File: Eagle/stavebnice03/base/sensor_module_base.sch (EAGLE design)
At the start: 5 parts

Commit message: I did an order in Eagle files
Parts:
- added C1, C3, C4, C5: 100nF, resistor:C-EUC0603
- added R1, R2, R4: 2k2, resistor:R-EU_R0603
- added R3: 2K2, resistor:R-EU_R0603
- added U$2, U$3, U$6, U$7: NC7SB3157P6X, !stavebnice03:NC7SB3157P6X
- added U$5: JUMPER5F-90, !stavebnice03:JUMPER5F-90
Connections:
- new net N$1: U$1.RA4, U$6.S, U$7.S
- new net N$10: R2.1, U$5.2, U$6.B0, U$7.B1
- new net N$20: U$2.B0, U$7.A
- new net N$4: U$1.RC1, U$3.A
- new net N$6: R1.1, U$5.4, U$6.B1, U$7.B0
- new net N$7: U$3.B0, U$6.A
- new net N$8: R4.1, U$3.B1, U$4.2
- new net N$9: U$1.RA5, U$2.S, U$3.S
- net GND: now also C1.2, C3.1, C4.2, C5.1, U$2.GND, U$3.GND, U$5.1, U$5.5, U$6.GND, U$7.GND
- net N$2: now also U$2.A; no longer U$4.2
- net N$5: now also R3.1, U$2.B1; no longer U$1.RC1
- net VCC: now also C1.1, C3.2, C4.1, C5.2, R1.2, R2.2, R3.2, R4.2, U$2.VCC, U$3.VCC, U$5.3, U$6.VCC, U$7.VCC; no longer U$1.RA4, U$1.RA5

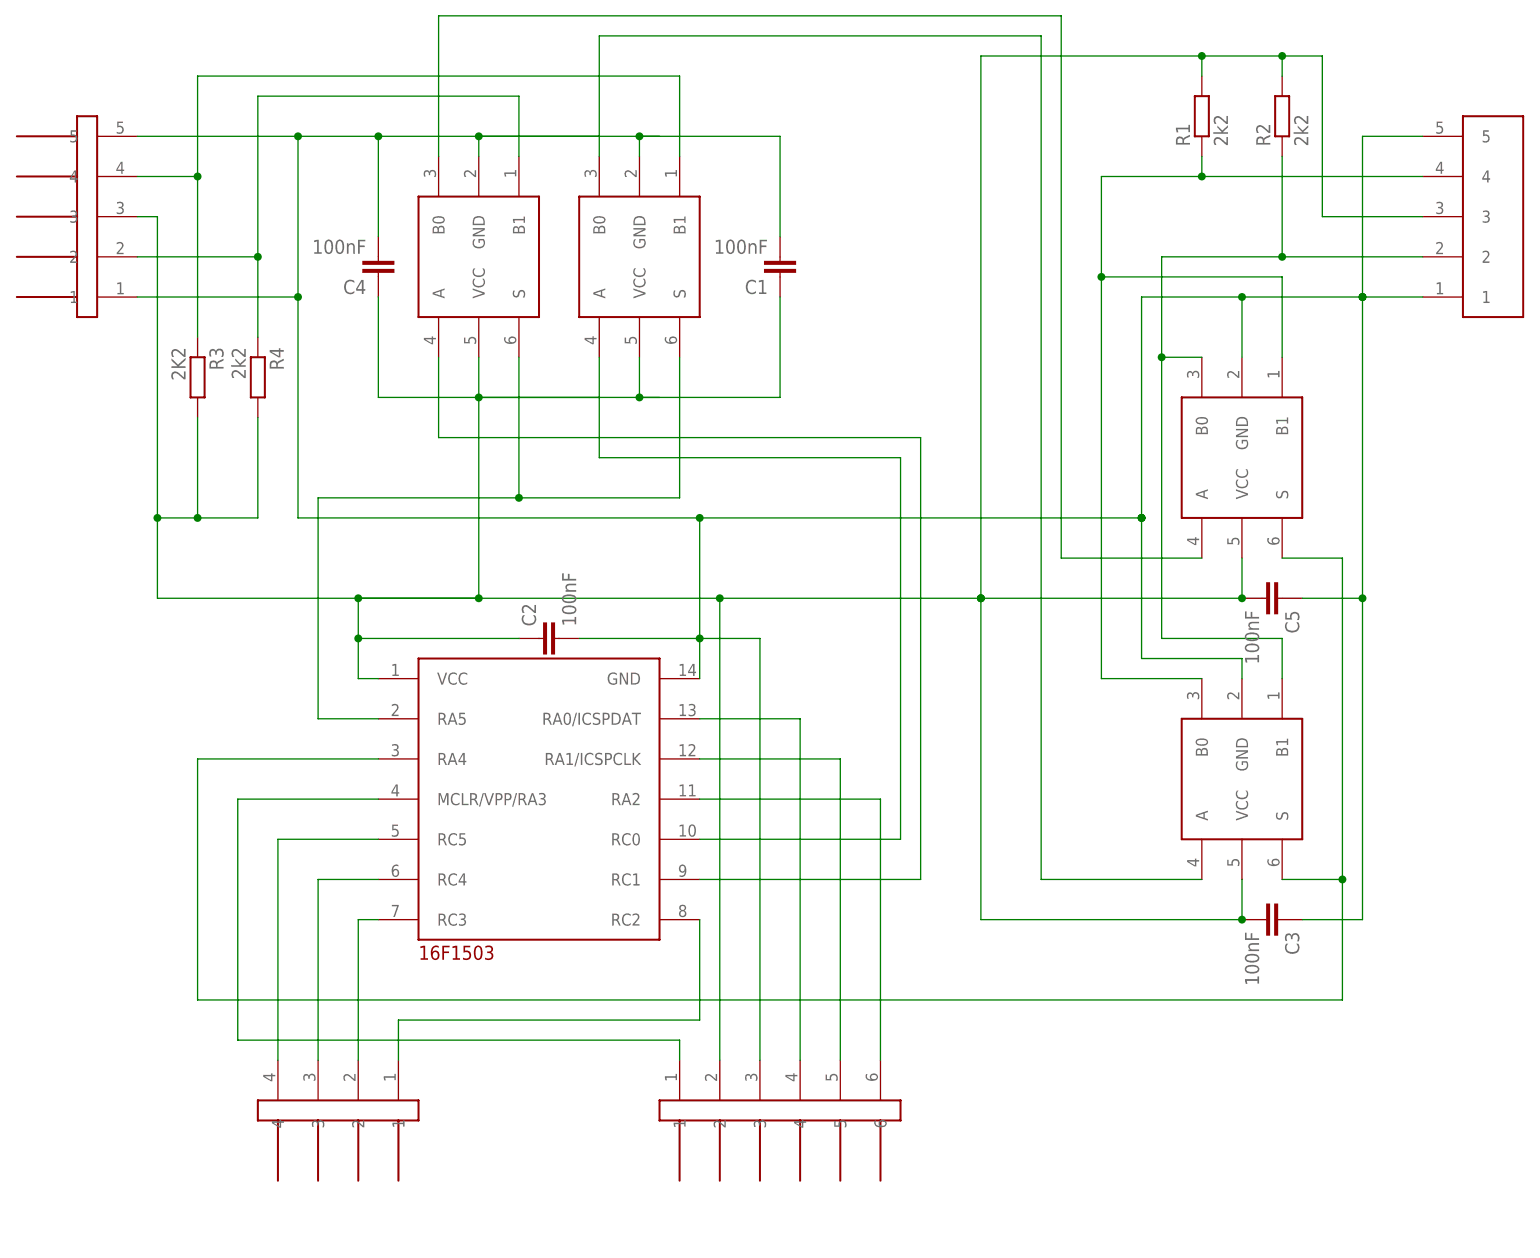
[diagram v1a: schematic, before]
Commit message: added wire from input bus to an iterrupt pin
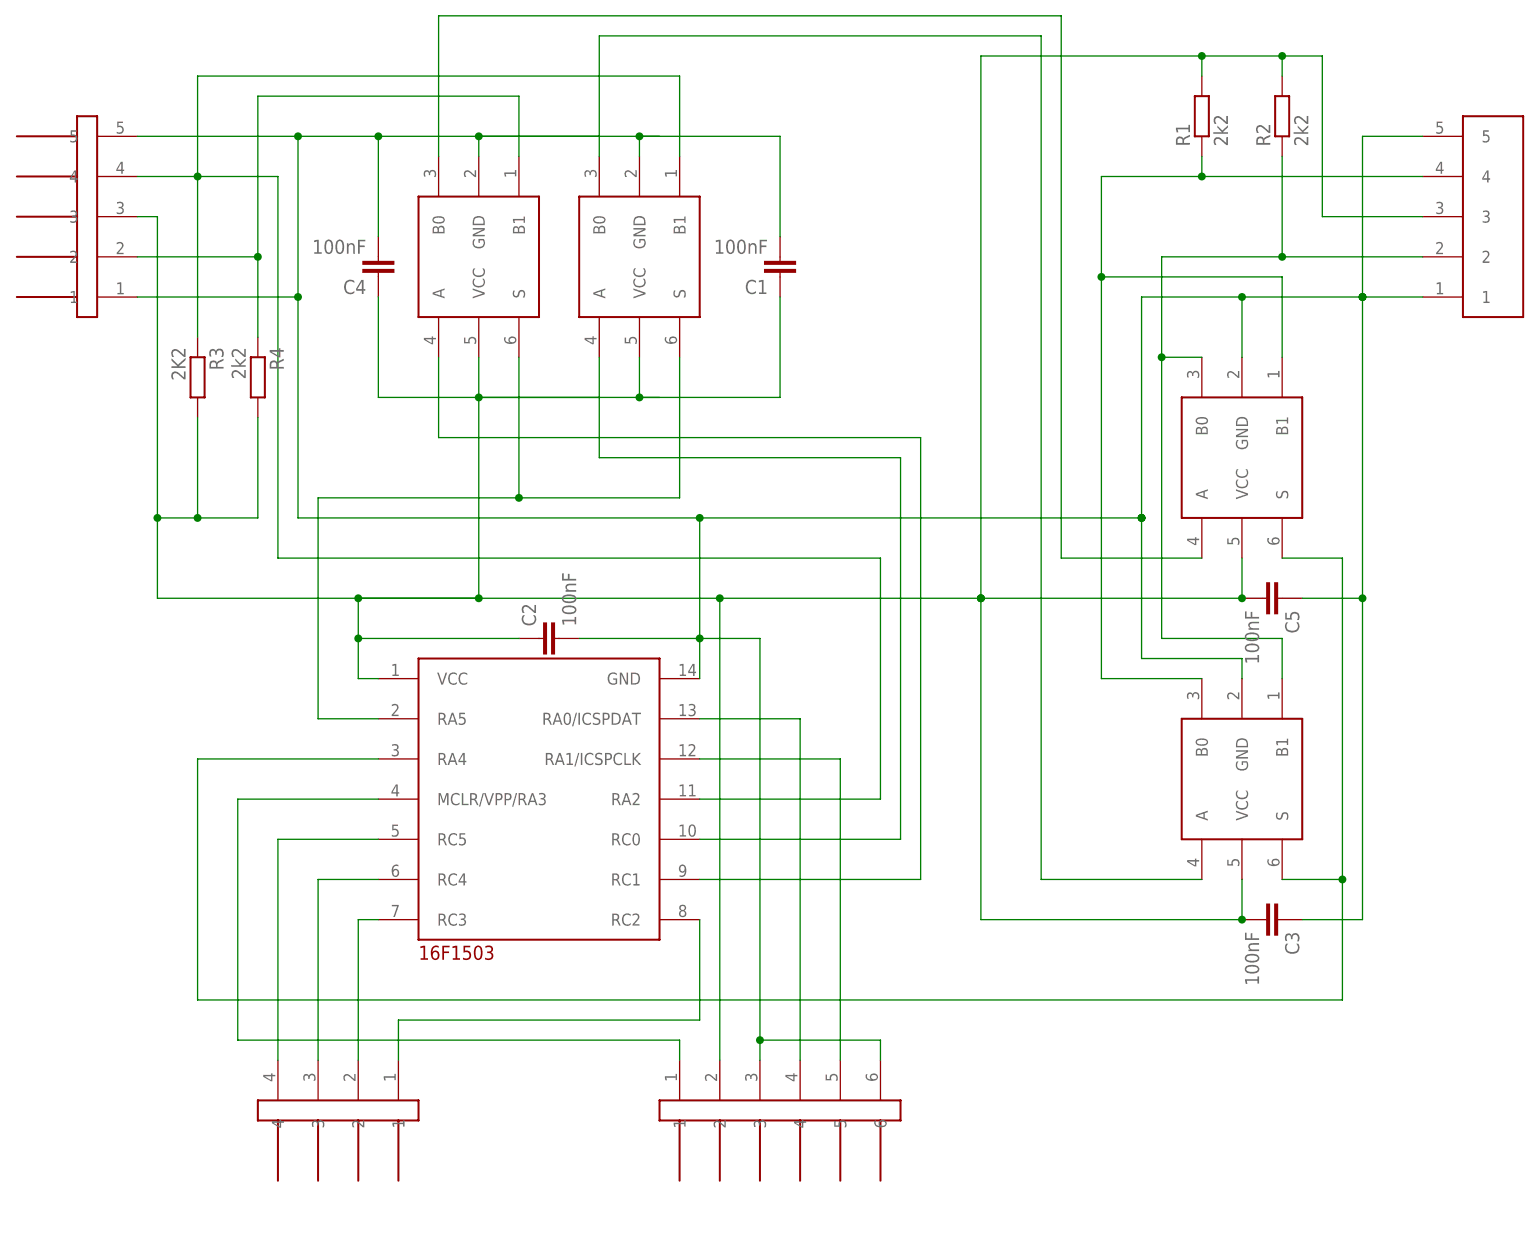
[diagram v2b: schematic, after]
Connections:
- removed net N$5: R3.1, U$2.B1, U$4.4
- net GND: now also U$8.6
- net N$11: now also R3.1, U$2.B1, U$4.4; no longer U$8.6
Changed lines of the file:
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@@
 <wire x1="124.46" y1="167.64" x2="124.46" y2="154.94" width="0.1524" layer="91"/>
 <junction x="137.16" y="167.64"/>
-<wire x1="172.72" y1="50.8" x2="172.72" y2="104.14" width="0.1524" layer="91"/>
+<wire x1="172.72" y1="50.8" x2="172.72" y2="53.34" width="0.1524" layer="91"/>
+<wire x1="172.72" y1="53.34" x2="172.72" y2="104.14" width="0.1524" layer="91"/>
 <wire x1="165.1" y1="104.14" x2="172.72" y2="104.14" width="0.1524" layer="91"/>
 <pinref part="U$1" gate="G$1" pin="GND"/>
@@
 <junction x="124.46" y="167.64"/>
 <junction x="114.3" y="167.64"/>
+<pinref part="U$8" gate="G$1" pin="6"/>
+<wire x1="172.72" y1="53.34" x2="187.96" y2="53.34" width="0.1524" layer="91"/>
+<wire x1="187.96" y1="53.34" x2="187.96" y2="50.8" width="0.1524" layer="91"/>
+<junction x="172.72" y="53.34"/>
 </segment>
 </net>
@@
 <pinref part="U$1" gate="G$1" pin="RA2"/>
 <wire x1="165.1" y1="83.82" x2="187.96" y2="83.82" width="0.1524" layer="91"/>
-<wire x1="187.96" y1="83.82" x2="187.96" y2="50.8" width="0.1524" layer="91"/>
-<pinref part="U$8" gate="G$1" pin="6"/>
+<wire x1="187.96" y1="83.82" x2="187.96" y2="114.3" width="0.1524" layer="91"/>
+<wire x1="187.96" y1="114.3" x2="111.76" y2="114.3" width="0.1524" layer="91"/>
+<wire x1="111.76" y1="114.3" x2="111.76" y2="162.56" width="0.1524" layer="91"/>
+<wire x1="162.56" y1="165.1" x2="162.56" y2="175.26" width="0.1524" layer="91"/>
+<pinref part="U$2" gate="G$1" pin="B1"/>
+<pinref part="U$4" gate="G$1" pin="4"/>
+<wire x1="162.56" y1="175.26" x2="101.6" y2="175.26" width="0.1524" layer="91"/>
+<wire x1="101.6" y1="162.56" x2="93.98" y2="162.56" width="0.1524" layer="91"/>
+<pinref part="R3" gate="G$1" pin="1"/>
+<wire x1="101.6" y1="175.26" x2="101.6" y2="162.56" width="0.1524" layer="91"/>
+<wire x1="101.6" y1="162.56" x2="101.6" y2="142.24" width="0.1524" layer="91"/>
+<junction x="101.6" y="162.56"/>
+<wire x1="111.76" y1="162.56" x2="101.6" y2="162.56" width="0.1524" layer="91"/>
 </segment>
 </net>
@@
 </segment>
 </net>
-<net name="N$5" class="0">
-<segment>
-<wire x1="162.56" y1="165.1" x2="162.56" y2="175.26" width="0.1524" layer="91"/>
-<pinref part="U$2" gate="G$1" pin="B1"/>
-<pinref part="U$4" gate="G$1" pin="4"/>
-<wire x1="162.56" y1="175.26" x2="101.6" y2="175.26" width="0.1524" layer="91"/>
-<wire x1="101.6" y1="162.56" x2="93.98" y2="162.56" width="0.1524" layer="91"/>
-<pinref part="R3" gate="G$1" pin="1"/>
-<wire x1="101.6" y1="175.26" x2="101.6" y2="162.56" width="0.1524" layer="91"/>
-<wire x1="101.6" y1="162.56" x2="101.6" y2="142.24" width="0.1524" layer="91"/>
-<junction x="101.6" y="162.56"/>
-</segment>
-</net>

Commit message: added pin and resistor to stay in bootloader + changed size back to 21x21 mm
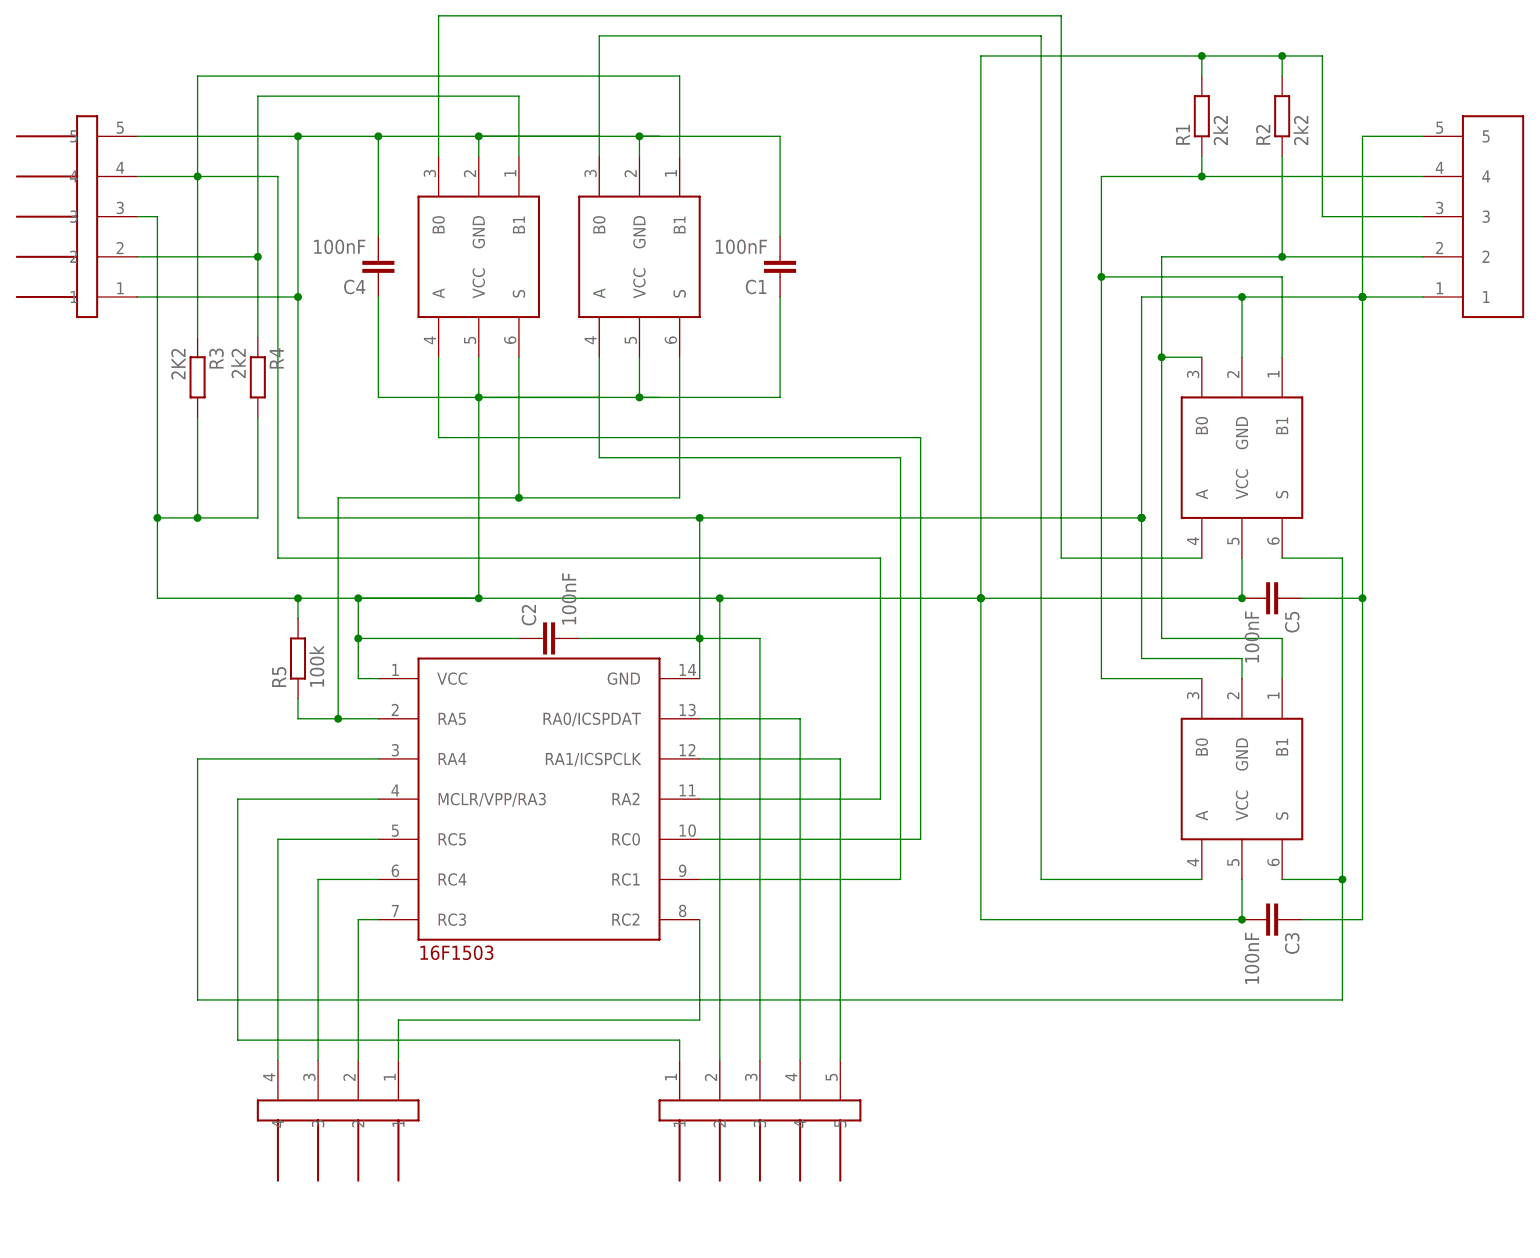
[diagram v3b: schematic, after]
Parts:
- added R5: 100k, resistor:R-EU_R0603
- U$8: value JUMPER6M -> JUMPER5M; device !stavebnice03:JUMPER6M -> !stavebnice03:JUMPER5M
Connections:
- net GND: no longer U$8.6
- net N$2: now also U$1.RC1; no longer U$1.RC0
- net N$4: now also U$1.RC0; no longer U$1.RC1
- net N$9: now also R5.1
- net VCC: now also R5.2
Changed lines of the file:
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@@
 <layer number="97" name="Info" color="7" fill="1" visible="yes" active="yes"/>
 <layer number="98" name="Guide" color="6" fill="1" visible="yes" active="yes"/>
+<layer number="99" name="SpiceOrder" color="5" fill="1" visible="no" active="no"/>
 </layers>
 <schematic xreflabel="%F%N/%S.%C%R" xrefpart="/%S.%C%R">
@@
 <part name="C5" library="resistor" deviceset="C-EU" device="C0603" value="100nF"/>
 <part name="C4" library="resistor" deviceset="C-EU" device="C0603" value="100nF"/>
-<part name="U$8" library="!stavebnice03" deviceset="JUMPER6M" device=""/>
 <part name="U$9" library="!stavebnice03" deviceset="JUMPER4M" device=""/>
 <part name="R3" library="resistor" deviceset="R-EU_" device="R0603" value="2K2"/>
 <part name="R4" library="resistor" deviceset="R-EU_" device="R0603" value="2k2"/>
+<part name="R5" library="resistor" deviceset="R-EU_" device="R0603" value="100k"/>
+<part name="U$8" library="!stavebnice03" deviceset="JUMPER5M" device=""/>
 </parts>
 <sheets>
@@
 <instance part="C5" gate="G$1" x="238.76" y="109.22" rot="R270"/>
 <instance part="C4" gate="G$1" x="124.46" y="149.86" rot="R180"/>
-<instance part="U$8" gate="G$1" x="175.26" y="43.18" rot="MR270"/>
 <instance part="U$9" gate="G$1" x="119.38" y="43.18" rot="R270"/>
 <instance part="R3" gate="G$1" x="101.6" y="137.16" rot="R270"/>
 <instance part="R4" gate="G$1" x="109.22" y="137.16" rot="R270"/>
+<instance part="R5" gate="G$1" x="114.3" y="101.6" rot="R90"/>
+<instance part="U$8" gate="G$1" x="172.72" y="43.18" rot="MR270"/>
 </instances>
 <busses>
@@
 <wire x1="124.46" y1="167.64" x2="124.46" y2="154.94" width="0.1524" layer="91"/>
 <junction x="137.16" y="167.64"/>
-<wire x1="172.72" y1="50.8" x2="172.72" y2="53.34" width="0.1524" layer="91"/>
-<wire x1="172.72" y1="53.34" x2="172.72" y2="104.14" width="0.1524" layer="91"/>
+<wire x1="172.72" y1="50.8" x2="172.72" y2="104.14" width="0.1524" layer="91"/>
 <wire x1="165.1" y1="104.14" x2="172.72" y2="104.14" width="0.1524" layer="91"/>
 <pinref part="U$1" gate="G$1" pin="GND"/>
@@
 <wire x1="157.48" y1="165.1" x2="157.48" y2="167.64" width="0.1524" layer="91"/>
 <junction x="157.48" y="167.64"/>
-<pinref part="U$8" gate="G$1" pin="3"/>
 <junction x="248.92" y="147.32"/>
 <junction x="124.46" y="167.64"/>
 <junction x="114.3" y="167.64"/>
-<pinref part="U$8" gate="G$1" pin="6"/>
-<wire x1="172.72" y1="53.34" x2="187.96" y2="53.34" width="0.1524" layer="91"/>
-<wire x1="187.96" y1="53.34" x2="187.96" y2="50.8" width="0.1524" layer="91"/>
-<junction x="172.72" y="53.34"/>
+<pinref part="U$8" gate="G$1" pin="3"/>
 </segment>
 </net>
@@
 <wire x1="167.64" y1="109.22" x2="137.16" y2="109.22" width="0.1524" layer="91"/>
 <wire x1="121.92" y1="109.22" x2="137.16" y2="109.22" width="0.1524" layer="91"/>
-<wire x1="137.16" y1="109.22" x2="96.52" y2="109.22" width="0.1524" layer="91"/>
+<wire x1="137.16" y1="109.22" x2="114.3" y2="109.22" width="0.1524" layer="91"/>
+<wire x1="114.3" y1="109.22" x2="96.52" y2="109.22" width="0.1524" layer="91"/>
 <wire x1="96.52" y1="109.22" x2="96.52" y2="119.38" width="0.1524" layer="91"/>
 <wire x1="96.52" y1="157.48" x2="93.98" y2="157.48" width="0.1524" layer="91"/>
@@
 <wire x1="157.48" y1="139.7" x2="157.48" y2="134.62" width="0.1524" layer="91"/>
 <junction x="157.48" y="134.62"/>
-<pinref part="U$8" gate="G$1" pin="2"/>
 <wire x1="96.52" y1="157.48" x2="96.52" y2="119.38" width="0.1524" layer="91"/>
 <pinref part="R4" gate="G$1" pin="2"/>
@@
 <junction x="101.6" y="119.38"/>
 <junction x="96.52" y="119.38"/>
+<pinref part="U$8" gate="G$1" pin="2"/>
+<pinref part="R5" gate="G$1" pin="2"/>
+<wire x1="114.3" y1="106.68" x2="114.3" y2="109.22" width="0.1524" layer="91"/>
+<junction x="114.3" y="109.22"/>
 </segment>
 </net>
@@
 <wire x1="162.56" y1="139.7" x2="162.56" y2="121.92" width="0.1524" layer="91"/>
 <pinref part="U$1" gate="G$1" pin="RA5"/>
-<wire x1="124.46" y1="93.98" x2="116.84" y2="93.98" width="0.1524" layer="91"/>
-<wire x1="116.84" y1="93.98" x2="116.84" y2="121.92" width="0.1524" layer="91"/>
-<wire x1="116.84" y1="121.92" x2="142.24" y2="121.92" width="0.1524" layer="91"/>
+<wire x1="124.46" y1="93.98" x2="119.38" y2="93.98" width="0.1524" layer="91"/>
+<wire x1="119.38" y1="93.98" x2="119.38" y2="121.92" width="0.1524" layer="91"/>
+<wire x1="119.38" y1="121.92" x2="142.24" y2="121.92" width="0.1524" layer="91"/>
 <pinref part="U$3" gate="G$1" pin="S"/>
 <wire x1="142.24" y1="139.7" x2="142.24" y2="121.92" width="0.1524" layer="91"/>
 <wire x1="162.56" y1="121.92" x2="142.24" y2="121.92" width="0.1524" layer="91"/>
 <junction x="142.24" y="121.92"/>
+<pinref part="R5" gate="G$1" pin="1"/>
+<wire x1="114.3" y1="96.52" x2="114.3" y2="93.98" width="0.1524" layer="91"/>
+<wire x1="114.3" y1="93.98" x2="119.38" y2="93.98" width="0.1524" layer="91"/>
+<junction x="119.38" y="93.98"/>
 </segment>
 </net>
@@
 <net name="N$4" class="0">
 <segment>
-<wire x1="193.04" y1="73.66" x2="193.04" y2="129.54" width="0.1524" layer="91"/>
 <pinref part="U$3" gate="G$1" pin="A"/>
+<wire x1="193.04" y1="78.74" x2="193.04" y2="129.54" width="0.1524" layer="91"/>
 <wire x1="193.04" y1="129.54" x2="132.08" y2="129.54" width="0.1524" layer="91"/>
 <wire x1="132.08" y1="129.54" x2="132.08" y2="139.7" width="0.1524" layer="91"/>
-<pinref part="U$1" gate="G$1" pin="RC1"/>
-<wire x1="165.1" y1="73.66" x2="193.04" y2="73.66" width="0.1524" layer="91"/>
+<pinref part="U$1" gate="G$1" pin="RC0"/>
+<wire x1="165.1" y1="78.74" x2="193.04" y2="78.74" width="0.1524" layer="91"/>
 </segment>
 </net>
@@
 <wire x1="152.4" y1="127" x2="152.4" y2="139.7" width="0.1524" layer="91"/>
 <wire x1="152.4" y1="127" x2="190.5" y2="127" width="0.1524" layer="91"/>
-<wire x1="190.5" y1="127" x2="190.5" y2="78.74" width="0.1524" layer="91"/>
-<pinref part="U$1" gate="G$1" pin="RC0"/>
-<wire x1="190.5" y1="78.74" x2="165.1" y2="78.74" width="0.1524" layer="91"/>
-</segment>
-</net>
+<wire x1="190.5" y1="127" x2="190.5" y2="73.66" width="0.1524" layer="91"/>
+<pinref part="U$1" gate="G$1" pin="RC1"/>
+<wire x1="190.5" y1="73.66" x2="165.1" y2="73.66" width="0.1524" layer="91"/>
+</segment>
+</net>
